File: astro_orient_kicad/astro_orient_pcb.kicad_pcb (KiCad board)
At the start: 2 copper layers, 82.5 x 48.5 mm, 36 parts, among them J1 BME260, J2 SWD_Tag_Connect, J3 USB-C_Receptacle, J4 test_points, SW1 SW_SPST, SW2 SW_Reset, SW3 SW_Boot, U1 STM32F072CBTx, U2 AP2112K-3.3, Y1 osc_crystal

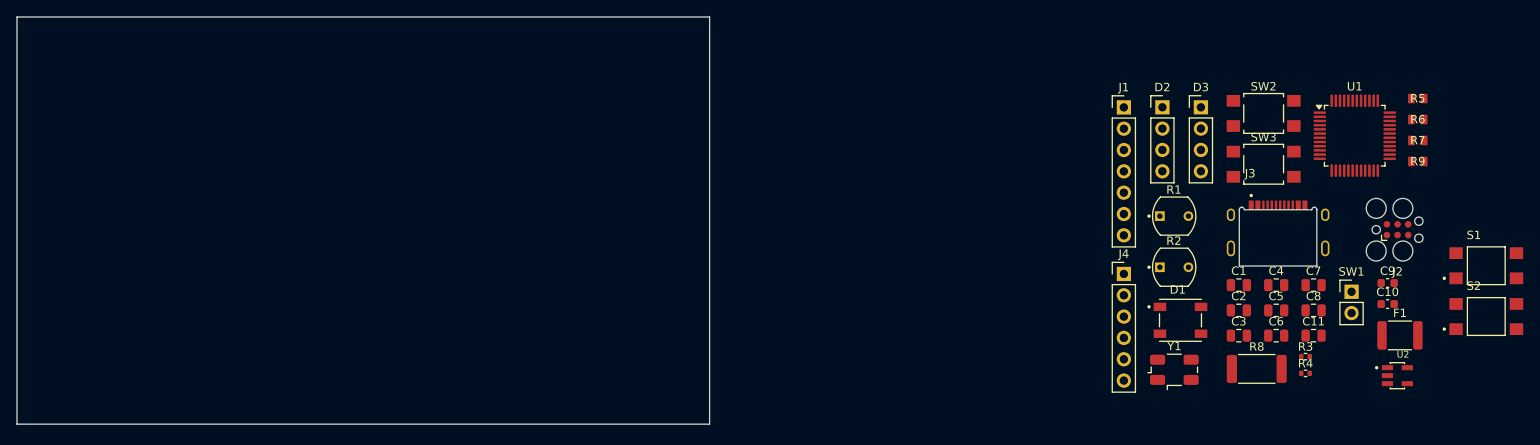
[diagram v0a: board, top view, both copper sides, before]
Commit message: updated schematic, partial layout of PCB
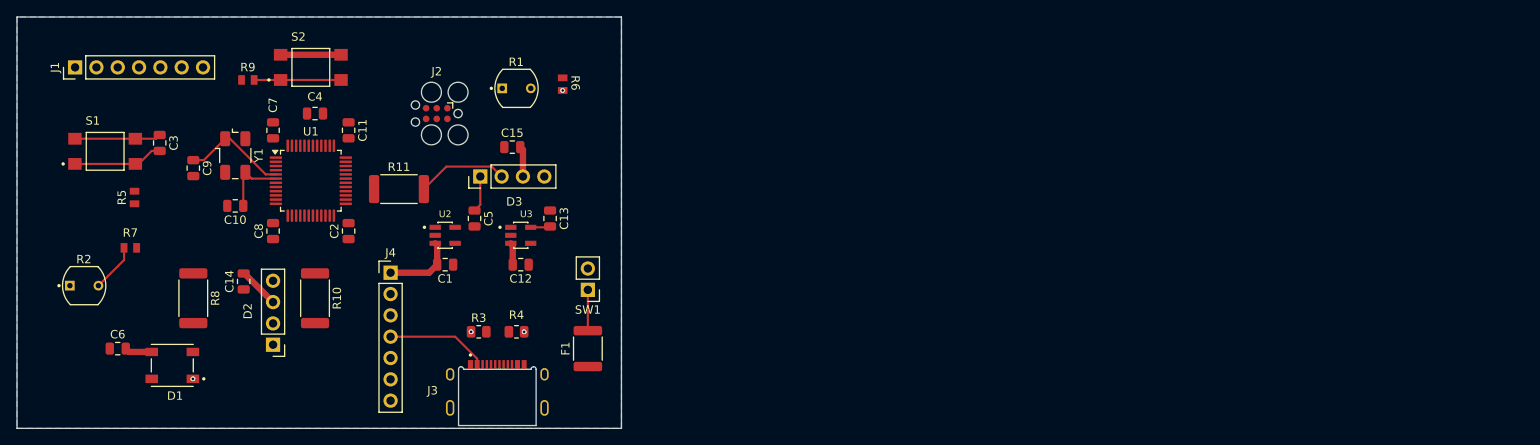
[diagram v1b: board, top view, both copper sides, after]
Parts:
- removed SW2: SW_Reset, Button_Switch_SMD:SW_SPST_TL3305A
- removed SW3: SW_Boot, Button_Switch_SMD:SW_SPST_TL3305A
- added C12: 2.2u, Capacitor_SMD:C_0805_2012Metric, F.Cu at (76.5, 45.5)
- added C13: 2.2u, Capacitor_SMD:C_0805_2012Metric, F.Cu at (80.0, 40.0)
- added C14: 0.1u, Capacitor_SMD:C_0805_2012Metric, F.Cu at (43.5, 47.5)
- added C15: 0.1u, Capacitor_SMD:C_0805_2012Metric, F.Cu at (75.5, 31.5)
- added R10: 470, Resistor_SMD:R_2512_6332Metric, F.Cu at (52.0, 49.5)
- added R11: 470, Resistor_SMD:R_2512_6332Metric, F.Cu at (62.0, 36.5)
- added U3: AP2112K-3.3, imported_footprints:SOT95P285X140-5N, F.Cu at (76.5, 42.0)
- C10, C9: footprint Capacitor_SMD:C_0603_1608Metric -> Capacitor_SMD:C_0805_2012Metric
- J4: footprint Connector_PinHeader_2.54mm:PinHeader_1x06_P2.54mm_Vertical -> Connector_PinHeader_2.54mm:PinHeader_1x07_P2.54mm_Vertical
- R3, R4: footprint Resistor_SMD:R_0402_1005Metric -> Resistor_SMD:R_0805_2012Metric
- moved S1 165.1 mm to (27.0, 32.0)
- moved R7 153.9 mm to (30.0, 43.5), turned to 180 degrees
- moved R5 153.3 mm to (30.5, 37.5), turned to 90 degrees
- moved S2 143.1 mm to (51.5, 22.0)
- moved C9 142.9 mm to (37.5, 34.0), turned to -90 degrees
- moved R9 139.7 mm to (44.0, 23.5)
- moved C6 138.0 mm to (28.5, 55.5)
- moved C10 137.8 mm to (42.5, 38.5), turned to 180 degrees
- moved C3 130.6 mm to (33.5, 31.0), turned to -90 degrees
- moved R2 129.9 mm to (24.5, 48.0)
- moved R8 127.0 mm to (37.5, 49.5), turned to -90 degrees
- moved C7 125.3 mm to (47.0, 29.5), turned to -90 degrees
- moved J1 125.0 mm to (23.4, 22.0), turned to 90 degrees
- moved U1 124.5 mm to (51.5, 35.5)
- moved C8 124.3 mm to (47.0, 41.5), turned to 90 degrees
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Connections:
- net /led_in renamed /led_1
- C11 pad 2: +3.3V -> +3.3V_Analog
- C8 pad 2: +3.3V -> +3.3V_Analog
- D1 pad 4: Net-(D1-DOUT) -> unconnected-(D1-DOUT-Pad4)
- D2 pad 2: Net-(D1-DOUT) -> Net-(D2-DIN)
- D2 pad 4: Net-(D2-DOUT) -> unconnected-(D2-DOUT-Pad4)
- D3 pad 2: Net-(D2-DOUT) -> Net-(D3-DIN)
- J4 pad 2: +3.3V -> +3.3V_Analog
- J4 pad 3: /VBUS -> +3.3V
- J4 pad 4: /USB_D+ -> /VBUS
- J4 pad 5: /USB_D- -> /USB_D+
- J4 pad 6: GND -> /USB_D-
- R1 pad 1: +3.3V -> +3.3V_Analog
- R2 pad 1: +3.3V -> +3.3V_Analog
- U1 pad 18: unconnected-(U1-PB0-Pad18) -> /led_2
- U1 pad 19: unconnected-(U1-PB1-Pad19) -> /led_3
- U1 pad 36: +3.3V -> +3.3V_Analog
- U1 pad 9: +3.3V -> +3.3V_Analog
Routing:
- net +5V: track 0.00 -> 23.1 mm
- net GND: track 0.00 -> 14.7 mm, vias 0 -> 4
- net /osc_in: track 0.00 -> 12.7 mm
- net /VBUS: track 0.00 -> 12.0 mm
- net Net-(D3-DIN): track 0.00 -> 10.9 mm
- net /RST: track 0.00 -> 10.7 mm
- net /BOOT: track 0.00 -> 10.4 mm
- net /osc_out: track 0.00 -> 8.05 mm
- net +3.3V: track 0.00 -> 7.20 mm
- net /photoresis_2: track 0.00 -> 5.76 mm
- net Net-(SW1-A): track 0.00 -> 4.86 mm
- net +3.3V_Analog: track 0.00 -> 2.36 mm
- net Net-(J3-CC2): track 0.00 -> 0.53 mm
- added copper zone on B.Cu, net GND
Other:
- board size 82.5 x 48.5 mm -> 72 x 49 mm

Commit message: completed layout of schematic
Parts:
- removed J4: test_points, Connector_PinHeader_2.54mm:PinHeader_1x07_P2.54mm_Vertical
- added TP1: GND_TP, TestPoint:TestPoint_Pad_D1.0mm, F.Cu at (70.2, 20.8)
- added TP2: 5V_TP, TestPoint:TestPoint_Pad_D1.0mm, F.Cu at (23.7, 61.2)
- added TP3: 3.3V_TP, TestPoint:TestPoint_Pad_D1.0mm, F.Cu at (74.5, 20.8)
- added TP4: 3.3V_A_TP, TestPoint:TestPoint_Pad_D1.0mm, F.Cu at (71.5, 57.2)
- added TP7: VBUS_TP, TestPoint:TestPoint_Pad_D1.0mm, F.Cu at (37.4, 59.7)
- C13, C5: value 2.2u -> 10u; footprint Capacitor_SMD:C_0805_2012Metric -> Capacitor_SMD:C_1206_3216Metric
- J3: footprint imported_footprints:SAMESKY_UJ20-C-H-G-MSMT-P16-TR -> imported_footprints:SAMESKY_UJ20-C-H-G-SMT-1-P16-TR_Correct
- moved J1 58.9 mm to (81.6, 30.9), turned to 0 degrees
- moved D3 50.7 mm to (21.0, 35.8), turned to 180 degrees
- moved C15 48.7 mm to (26.9, 29.9), turned to 180 degrees
- moved C13 42.0 mm to (38.4, 46.0)
- moved U3 34.9 mm to (42.5, 49.9), turned to 180 degrees
- moved R5 34.4 mm to (62.8, 25.7)
- moved C12 33.5 mm to (43.0, 46.0), turned to 0 degrees
- moved R1 32.5 mm to (78.9, 56.9)
- moved C3 31.2 mm to (62.9, 20.7)
- moved R9 31.1 mm to (73.6, 33.0), turned to 180 degrees
- moved S1 31.0 mm to (56.9, 23.6)
- moved R6 30.9 mm to (70.5, 52.9), turned to 180 degrees
- moved R11 28.7 mm to (33.5, 33.4), turned to 180 degrees
- moved R3 28.4 mm to (43.4, 57.9), turned to 90 degrees
- moved D2 26.8 mm to (21.1, 48.2)
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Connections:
- U1 pad 16: /led_1 -> /led_3
- U1 pad 19: /led_3 -> /led_1
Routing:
- net +3.3V_Analog: track 2.36 -> 94.2 mm, vias 0 -> 3
- net +3.3V: track 7.20 -> 96.1 mm, vias 0 -> 4
- net +5V: track 23.1 -> 97.1 mm, vias 0 -> 2
- net /photoresis_1: track 0.00 -> 45.9 mm, vias 0 -> 2
- net /RST: track 10.7 -> 51.1 mm, vias 0 -> 4
- net /sensor_SDI: track 0.00 -> 31.7 mm, vias 0 -> 1
- net /sensor_SCK: track 0.00 -> 29.4 mm, vias 0 -> 1
- net /SWDIO: track 0.00 -> 25.6 mm
- net /photoresis_2: track 5.76 -> 28.2 mm
- net /led_1: track 0.00 -> 22.3 mm
- net /USB_D+: track 0.00 -> 22.1 mm
- net GND: track 14.7 -> 36.7 mm, vias 4 -> 9
- net /USB_D-: track 0.00 -> 22.0 mm
- net /VBUS: track 12.0 -> 33.4 mm
- net /SWCLK: track 0.00 -> 20.4 mm
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- added copper zone on F.Cu, net GND
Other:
- board text added: "3.3V"
- board text added: "3.3V_A"
- board text added: "5V"
- board text added: "GND"
- board text added: "VBUS"

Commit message: completed layout of schematic
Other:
- board text added: "astro_orient_kcg"
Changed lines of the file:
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@@
 		(layer "Edge.Cuts")
+	)
+	(gr_text "astro_orient_kcg\n"
+		(at 72.17 63.08 0)
+		(layer "F.SilkS")
+		(effects
+			(font
+				(size 1.2 1.2)
+				(thickness 0.15)
+			)
+			(justify left bottom)
+		)
 	)
 	(gr_text "3.3V_A\n"
@@
 	)
 	(segment
+		(start 49.47 28.25)
+		(end 48.800735 28.919265)
+		(width 0.2)
+		(layer "B.Cu")
+		(net 4)
+	)
+	(segment
+		(start 48.800735 28.919265)
+		(end 48.800735 29.099265)
+		(width 0.2)
+		(layer "B.Cu")
+		(net 4)
+	)
+	(segment
 		(start 50.55 28.25)
-		(end 49.700735 29.099265)
+		(end 49.47 28.25)
 		(width 0.2)
 		(layer "B.Cu")
@@
 		(width 0.2)
 		(layer "B.Cu")
-		(net 4)
-	)
-	(segment
-		(start 49.700735 29.099265)
-		(end 48.800735 29.099265)
-		(width 0.2)
-		(layer "B.Cu")

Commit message: last changes to PCB
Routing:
- net GND: track 36.7 -> 37.3 mm
